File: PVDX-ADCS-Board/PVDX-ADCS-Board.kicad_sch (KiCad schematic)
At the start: 56 parts, among them J1 Conn_01x36, J2 Conn_01x18, U1 OPA380AIDGKT, U10 OPA380AIDGKT, U11 OPA380AIDGKT, U12 OPA380AIDGKT, U13 OPA380AIDGKT, U14 OPA380AIDGKT, U15 OPA380AIDGKT, U16 OPA380AIDGKT, U17 OPA380AIDGKT, U18 OPA380AIDGKT, U2 OPA380AIDGKT, U3 OPA380AIDGKT, U4 OPA380AIDGKT, U5 OPA380AIDGKT, U6 OPA380AIDGKT, U7 OPA380AIDGKT, U8 OPA380AIDGKT, U9 OPA380AIDGKT

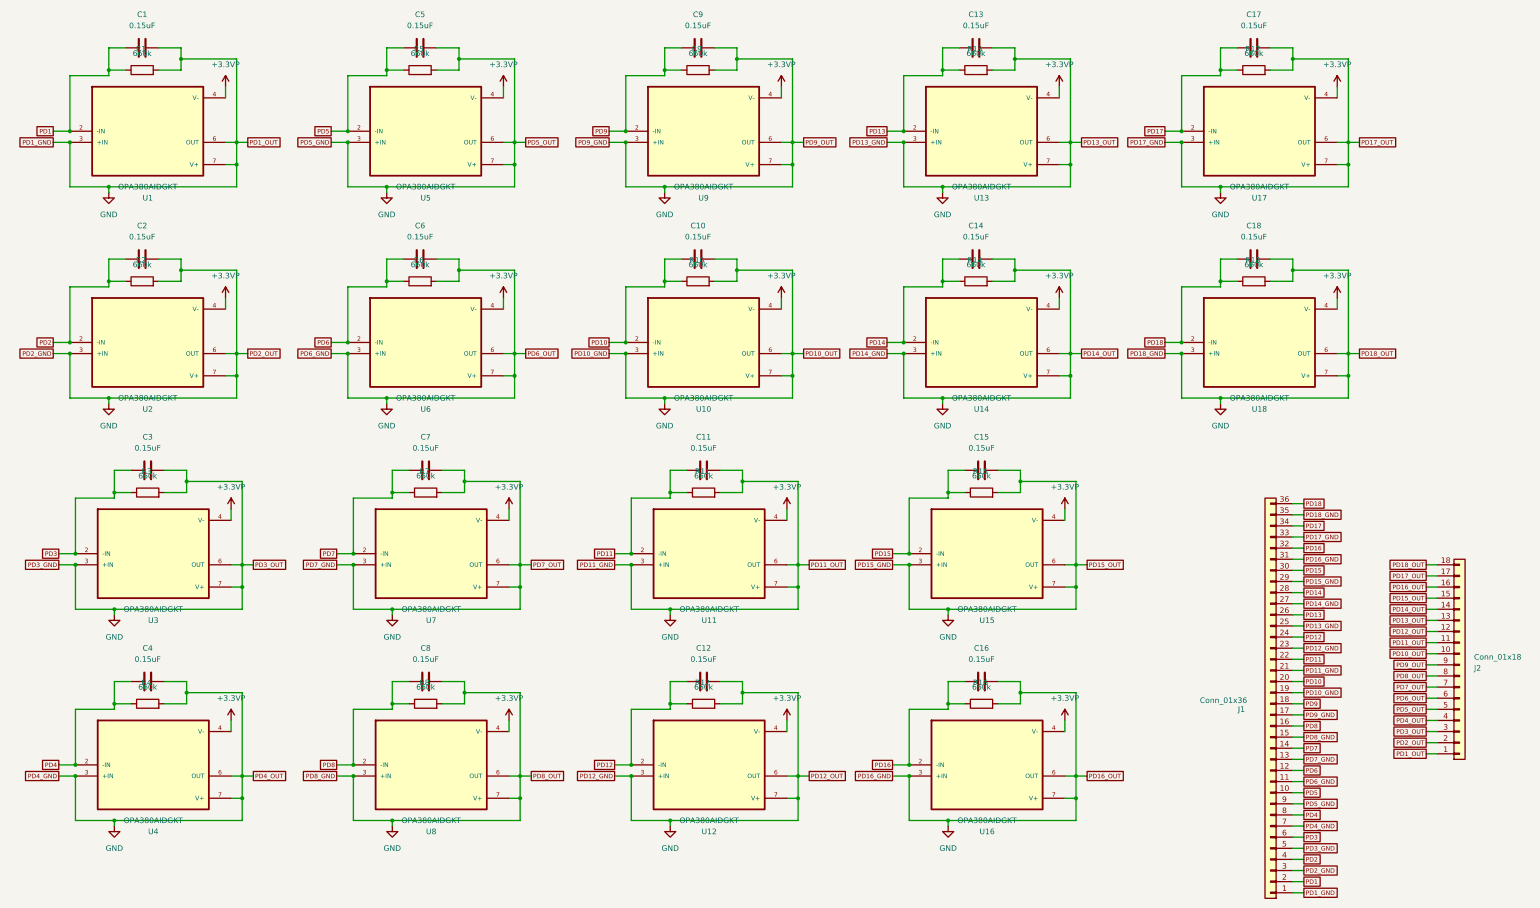
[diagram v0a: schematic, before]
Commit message: fixed wiring to gnd and readability of capacitor
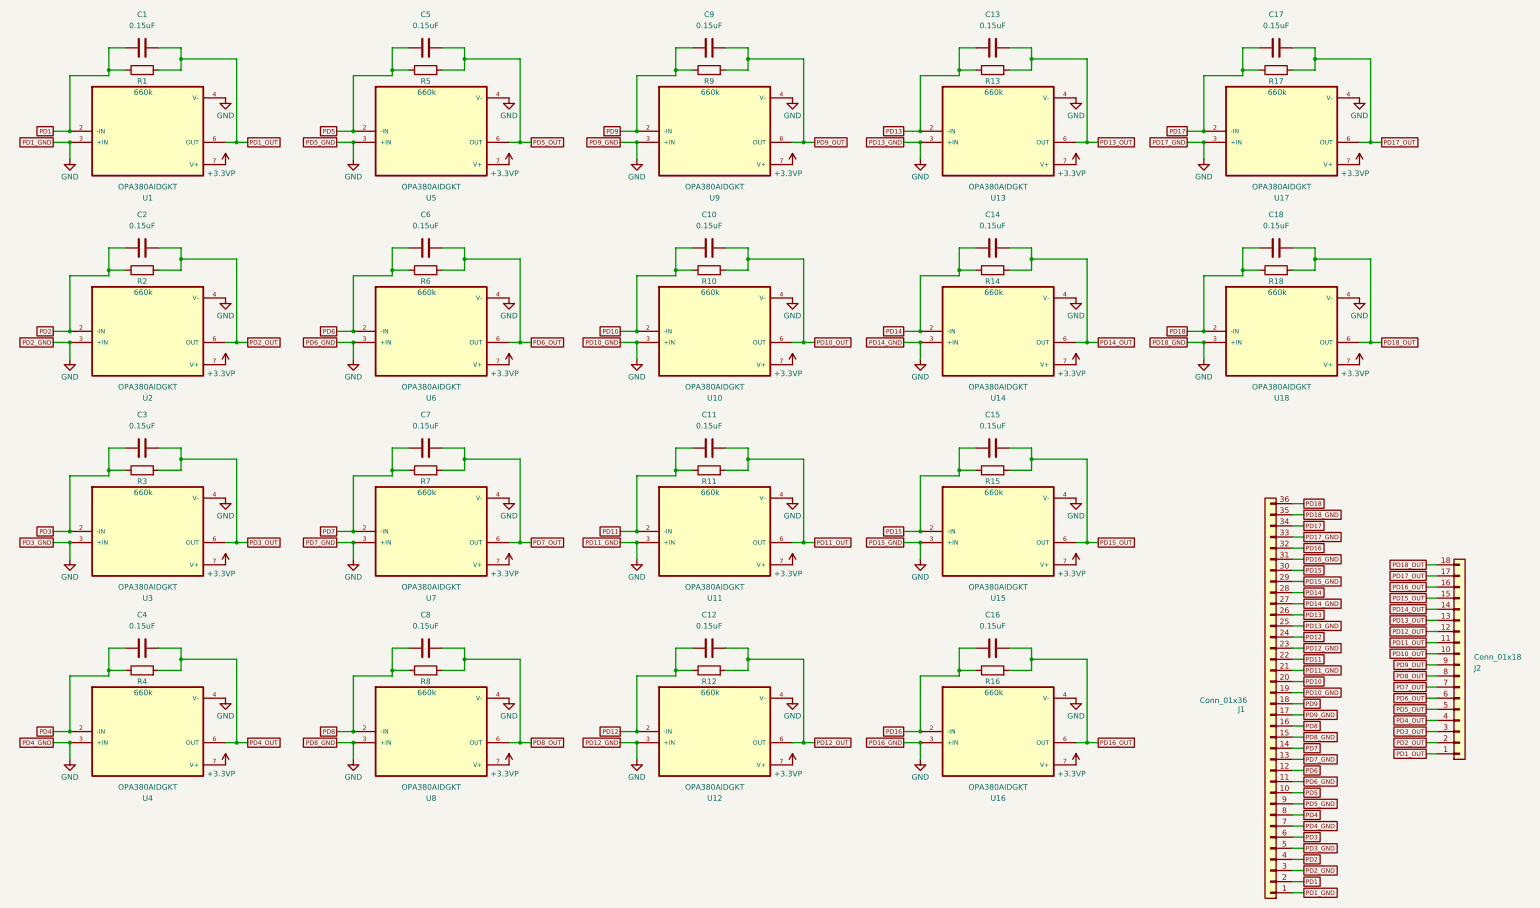
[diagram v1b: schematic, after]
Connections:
- net +3.3VP: now also U1.7 (V+), U10.7 (V+), U11.7 (V+), U12.7 (V+), U13.7 (V+), U14.7 (V+), U15.7 (V+), U16.7 (V+), U17.7 (V+), U18.7 (V+), U2.7 (V+), U3.7 (V+), U4.7 (V+), U5.7 (V+), U6.7 (V+), U7.7 (V+), U8.7 (V+), U9.7 (V+); no longer U1.4 (V-), U10.4 (V-), U11.4 (V-), U12.4 (V-), U13.4 (V-), U14.4 (V-), U15.4 (V-), U16.4 (V-), U17.4 (V-), U18.4 (V-), U2.4 (V-), U3.4 (V-), U4.4 (V-), U5.4 (V-), U6.4 (V-), U7.4 (V-), U8.4 (V-), U9.4 (V-)
- net GND: now also U1.4 (V-), U10.4 (V-), U11.4 (V-), U12.4 (V-), U13.4 (V-), U14.4 (V-), U15.4 (V-), U16.4 (V-), U17.4 (V-), U18.4 (V-), U2.4 (V-), U3.4 (V-), U4.4 (V-), U5.4 (V-), U6.4 (V-), U7.4 (V-), U8.4 (V-), U9.4 (V-); no longer C1.2, C10.2, C11.2, C12.2, C13.2, C14.2, C15.2, C16.2, C17.2, C18.2, C2.2, C3.2, C4.2, C5.2, C6.2, C7.2, C8.2, C9.2, J2.1 (Pin_1), J2.10 (Pin_10), J2.11 (Pin_11), J2.12 (Pin_12), J2.13 (Pin_13), J2.14 (Pin_14), J2.15 (Pin_15), J2.16 (Pin_16), J2.17 (Pin_17), J2.18 (Pin_18), J2.2 (Pin_2), J2.3 (Pin_3), J2.4 (Pin_4), J2.5 (Pin_5), J2.6 (Pin_6), J2.7 (Pin_7), J2.8 (Pin_8), J2.9 (Pin_9), R1.2, R10.2, R11.2, R12.2, R13.2, R14.2, R15.2, R16.2, R17.2, R18.2, R2.2, R3.2, R4.2, R5.2, R6.2, R7.2, R8.2, R9.2, U1.6 (OUT), U1.7 (V+), U10.6 (OUT), U10.7 (V+), U11.6 (OUT), U11.7 (V+), U12.6 (OUT), U12.7 (V+), U13.6 (OUT), U13.7 (V+), U14.6 (OUT), U14.7 (V+), U15.6 (OUT), U15.7 (V+), U16.6 (OUT), U16.7 (V+), U17.6 (OUT), U17.7 (V+), U18.6 (OUT), U18.7 (V+), U2.6 (OUT), U2.7 (V+), U3.6 (OUT), U3.7 (V+), U4.6 (OUT), U4.7 (V+), U5.6 (OUT), U5.7 (V+), U6.6 (OUT), U6.7 (V+), U7.6 (OUT), U7.7 (V+), U8.6 (OUT), U8.7 (V+), U9.6 (OUT), U9.7 (V+)
- new net PD10_OUT: C10.2, J2.10 (Pin_10), R10.2, U10.6 (OUT)
- new net PD11_OUT: C11.2, J2.11 (Pin_11), R11.2, U11.6 (OUT)
- new net PD12_OUT: C12.2, J2.12 (Pin_12), R12.2, U12.6 (OUT)
- new net PD13_OUT: C13.2, J2.13 (Pin_13), R13.2, U13.6 (OUT)
- new net PD14_OUT: C14.2, J2.14 (Pin_14), R14.2, U14.6 (OUT)
- new net PD15_OUT: C15.2, J2.15 (Pin_15), R15.2, U15.6 (OUT)
- new net PD16_OUT: C16.2, J2.16 (Pin_16), R16.2, U16.6 (OUT)
- new net PD17_OUT: C17.2, J2.17 (Pin_17), R17.2, U17.6 (OUT)
- new net PD18_OUT: C18.2, J2.18 (Pin_18), R18.2, U18.6 (OUT)
- new net PD1_OUT: C1.2, J2.1 (Pin_1), R1.2, U1.6 (OUT)
- new net PD2_OUT: C2.2, J2.2 (Pin_2), R2.2, U2.6 (OUT)
- new net PD3_OUT: C3.2, J2.3 (Pin_3), R3.2, U3.6 (OUT)
- new net PD4_OUT: C4.2, J2.4 (Pin_4), R4.2, U4.6 (OUT)
- new net PD5_OUT: C5.2, J2.5 (Pin_5), R5.2, U5.6 (OUT)
- new net PD6_OUT: C6.2, J2.6 (Pin_6), R6.2, U6.6 (OUT)
- new net PD7_OUT: C7.2, J2.7 (Pin_7), R7.2, U7.6 (OUT)
- new net PD8_OUT: C8.2, J2.8 (Pin_8), R8.2, U8.6 (OUT)
- new net PD9_OUT: C9.2, J2.9 (Pin_9), R9.2, U9.6 (OUT)
